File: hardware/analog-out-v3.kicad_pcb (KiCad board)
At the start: 2 copper layers, 30 x 35 mm, 41 parts, among them P1 DEBUG, P2 CONN_5, P3 CON-SENSOR2, P4 BOOT, U1 XMC1XXX24, U2 MCP4725A0, U3 TLV272IS, U4 DRILL, U5 DRILL, U6 DRILL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

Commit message: pullup 4k7->2k2, fix origin, fix logos
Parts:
- RP2: value 4k7 -> 2k2
- moved G*** 11.0 mm to (153.1, 100.1)
- moved VAL 10.6 mm to (153.1, 92.1)
- moved VAL 8.06 mm to (153.1, 108.1)
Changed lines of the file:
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@@
-(kicad_pcb (version 4) (host pcbnew 4.0.2+dfsg1-stable)
+(kicad_pcb (version 4) (host pcbnew 4.0.7-e2-6376~61~ubuntu18.04.1)
   (general
     (links 78)
     (no_connects 0)
-    (area 13.564138 81.720139 168.904861 194.555743)
+    (area 13.66415 81.720139 168.904861 194.955793)
     (thickness 1.6002)
     (drawings 23)
@@
   )
   (layers
-    (0 Vorderseite signal)
-    (31 Rückseite signal)
+    (0 Vorderseite signal hide)
+    (31 Rückseite signal hide)
     (32 B.Adhes user)
     (33 F.Adhes user)
@@
     (pad_drill 1.30048)
     (pad_to_mask_clearance 0)
-    (aux_axis_origin 138.05 117.575)
-    (grid_origin 138.05 117.575)
-    (visible_elements FFFFDFBF)
+    (aux_axis_origin 138.05 82.575)
+    (grid_origin 138.05 82.575)
+    (visible_elements FFFF9FBF)
     (pcbplotparams
       (layerselection 0x00030_80000001)
@@
   )
   (module kicad-libraries:CE_5mm (layer Rückseite)
-    (at 160.05 100.075 180)
+    (at 153.05 92.075 180)
     (fp_text reference VAL (at 0 0 180) (layer B.SilkS) hide
       (effects (font (size 0.2 0.2) (thickness 0.05)) (justify mirror))
@@
   )
   (module kicad-libraries:WEEE_7mm (layer Rückseite)
-    (at 152.05 100.075 180)
+    (at 153.05 108.075 180)
     (fp_text reference VAL (at 0 0 180) (layer B.SilkS) hide
       (effects (font (size 0.2 0.2) (thickness 0.05)) (justify mirror))
@@
       (effects (font (size 0.29972 0.29972) (thickness 0.07493)))
     )
-    (fp_text value 4k7 (at 1.01 -0.02) (layer F.Fab)
+    (fp_text value 2k2 (at 1.01 -0.02) (layer F.Fab)
       (effects (font (size 0.29972 0.29972) (thickness 0.07493)))
     )
@@
   )
   (module kicad-libraries:Logo_CoMCU (layer Rückseite)
-    (at 142.02 100.055 180)
+    (at 153.05 100.075 180)
     (fp_text reference G*** (at 0 0 180) (layer B.SilkS) hide
       (effects (font (thickness 0.3)) (justify mirror))

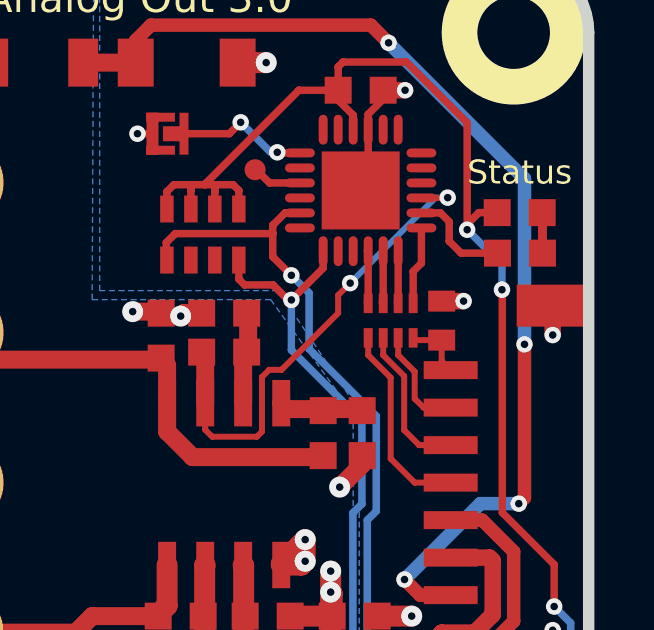
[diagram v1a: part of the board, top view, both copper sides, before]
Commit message: Change capacitor footprint(s) to C0402F
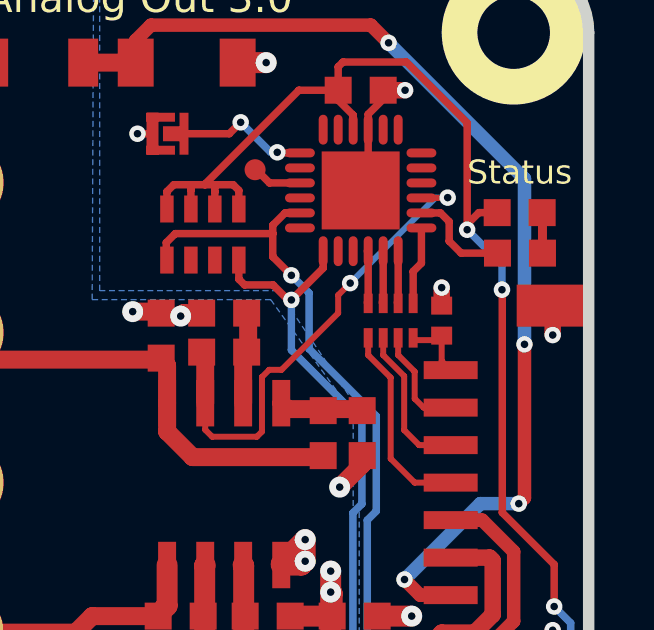
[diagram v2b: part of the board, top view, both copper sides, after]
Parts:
- C5: footprint kicad-libraries:C0402E -> kicad-libraries:C0402F
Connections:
- RP2 pad 6: (no net) -> Net-(RP2-Pad6)
- RP2 pad 7: (no net) -> Net-(RP2-Pad7)
- U1 pad 11: (no net) -> Net-(U1-Pad11)
- U1 pad 12: (no net) -> Net-(U1-Pad12)
- U1 pad 14: (no net) -> Net-(U1-Pad14)
- U1 pad 16: (no net) -> Net-(U1-Pad16)
- U1 pad 18: (no net) -> Net-(U1-Pad18)
- U1 pad 20: (no net) -> Net-(U1-Pad20)
- U1 pad 21: (no net) -> Net-(U1-Pad21)
- U1 pad 4: (no net) -> Net-(U1-Pad4)
- U1 pad 5: (no net) -> Net-(U1-Pad5)
- U1 pad 6: (no net) -> Net-(U1-Pad6)
- U1 pad 7: (no net) -> Net-(U1-Pad7)
- U1 pad 8: (no net) -> Net-(U1-Pad8)
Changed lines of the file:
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@@
-(kicad_pcb (version 4) (host pcbnew 4.0.7-e2-6376~61~ubuntu18.04.1)
+(kicad_pcb (version 4) (host pcbnew 4.0.2+dfsg1-stable)
   (general
     (links 78)
     (no_connects 0)
-    (area 13.66415 81.720139 168.904861 194.955793)
+    (area 13.564138 81.720139 168.904861 194.555743)
     (thickness 1.6002)
     (drawings 23)
@@
     (zones 0)
     (modules 41)
-    (nets 29)
+    (nets 43)
   )
   (page A4)
@@
   )
   (layers
-    (0 Vorderseite signal hide)
-    (31 Rückseite signal hide)
+    (0 Vorderseite signal)
+    (31 Rückseite signal)
     (32 B.Adhes user)
     (33 F.Adhes user)
@@
     (aux_axis_origin 138.05 82.575)
     (grid_origin 138.05 82.575)
-    (visible_elements FFFF9FBF)
+    (visible_elements FFFFDFBF)
     (pcbplotparams
       (layerselection 0x00030_80000001)
@@
   (net 27 S-CLK)
   (net 28 S-CS)
+  (net 29 "Net-(RP2-Pad6)")
+  (net 30 "Net-(RP2-Pad7)")
+  (net 31 "Net-(U1-Pad4)")
+  (net 32 "Net-(U1-Pad5)")
+  (net 33 "Net-(U1-Pad6)")
+  (net 34 "Net-(U1-Pad7)")
+  (net 35 "Net-(U1-Pad8)")
+  (net 36 "Net-(U1-Pad11)")
+  (net 37 "Net-(U1-Pad12)")
+  (net 38 "Net-(U1-Pad14)")
+  (net 39 "Net-(U1-Pad16)")
+  (net 40 "Net-(U1-Pad18)")
+  (net 41 "Net-(U1-Pad20)")
+  (net 42 "Net-(U1-Pad21)")
   (net_class Default "Dies ist die voreingestellte Netzklasse."
     (clearance 0.14986)
@@
     (add_net "Net-(R4-Pad2)")
     (add_net "Net-(R5-Pad1)")
+    (add_net "Net-(RP2-Pad6)")
+    (add_net "Net-(RP2-Pad7)")
+    (add_net "Net-(U1-Pad11)")
+    (add_net "Net-(U1-Pad12)")
+    (add_net "Net-(U1-Pad14)")
+    (add_net "Net-(U1-Pad16)")
+    (add_net "Net-(U1-Pad18)")
+    (add_net "Net-(U1-Pad20)")
+    (add_net "Net-(U1-Pad21)")
+    (add_net "Net-(U1-Pad4)")
+    (add_net "Net-(U1-Pad5)")
+    (add_net "Net-(U1-Pad6)")
+    (add_net "Net-(U1-Pad7)")
+    (add_net "Net-(U1-Pad8)")
     (add_net S-CLK)
     (add_net S-CS)
@@
     (pad 3 smd oval (at -2.025 -0.25 180) (size 1 0.3) (layers Vorderseite F.Paste F.Mask)
       (net 20 VIN))
-    (pad 4 smd oval (at -2.025 0.25 180) (size 1 0.3) (layers Vorderseite F.Paste F.Mask))
-    (pad 5 smd oval (at -2.025 0.75 180) (size 1 0.3) (layers Vorderseite F.Paste F.Mask))
-    (pad 6 smd oval (at -2.025 1.25 180) (size 1 0.3) (layers Vorderseite F.Paste F.Mask))
-    (pad 7 smd oval (at -1.25 2.025 270) (size 1 0.3) (layers Vorderseite F.Paste F.Mask))
-    (pad 8 smd oval (at -0.75 2.025 270) (size 1 0.3) (layers Vorderseite F.Paste F.Mask))
+    (pad 4 smd oval (at -2.025 0.25 180) (size 1 0.3) (layers Vorderseite F.Paste F.Mask)
+      (net 31 "Net-(U1-Pad4)"))
+    (pad 5 smd oval (at -2.025 0.75 180) (size 1 0.3) (layers Vorderseite F.Paste F.Mask)
+      (net 32 "Net-(U1-Pad5)"))
+    (pad 6 smd oval (at -2.025 1.25 180) (size 1 0.3) (layers Vorderseite F.Paste F.Mask)
+      (net 33 "Net-(U1-Pad6)"))
+    (pad 7 smd oval (at -1.25 2.025 270) (size 1 0.3) (layers Vorderseite F.Paste F.Mask)
+      (net 34 "Net-(U1-Pad7)"))
+    (pad 8 smd oval (at -0.75 2.025 270) (size 1 0.3) (layers Vorderseite F.Paste F.Mask)
+      (net 35 "Net-(U1-Pad8)"))
     (pad 9 smd oval (at -0.25 2.025 270) (size 1 0.3) (layers Vorderseite F.Paste F.Mask)
       (net 2 GND))
     (pad 10 smd oval (at 0.25 2.025 270) (size 1 0.3) (layers Vorderseite F.Paste F.Mask)
       (net 7 3V3))
-    (pad 11 smd oval (at 0.75 2.025 270) (size 1 0.3) (layers Vorderseite F.Paste F.Mask))
-    (pad 12 smd oval (at 1.25 2.025 270) (size 1 0.3) (layers Vorderseite F.Paste F.Mask))
+    (pad 11 smd oval (at 0.75 2.025 270) (size 1 0.3) (layers Vorderseite F.Paste F.Mask)
+      (net 36 "Net-(U1-Pad11)"))
+    (pad 12 smd oval (at 1.25 2.025 270) (size 1 0.3) (layers Vorderseite F.Paste F.Mask)
+      (net 37 "Net-(U1-Pad12)"))
     (pad 13 smd oval (at 2.025 1.25 180) (size 1 0.3) (layers Vorderseite F.Paste F.Mask)
       (net 19 "Net-(P4-Pad2)"))
-    (pad 14 smd oval (at 2.025 0.75 180) (size 1 0.3) (layers Vorderseite F.Paste F.Mask))
+    (pad 14 smd oval (at 2.025 0.75 180) (size 1 0.3) (layers Vorderseite F.Paste F.Mask)
+      (net 38 "Net-(U1-Pad14)"))
     (pad 15 smd oval (at 2.025 0.25 180) (size 1 0.3) (layers Vorderseite F.Paste F.Mask)
       (net 18 "Net-(P1-Pad1)"))
-    (pad 16 smd oval (at 2.025 -0.25 180) (size 1 0.3) (layers Vorderseite F.Paste F.Mask))
+    (pad 16 smd oval (at 2.025 -0.25 180) (size 1 0.3) (layers Vorderseite F.Paste F.Mask)
+      (net 39 "Net-(U1-Pad16)"))
     (pad 17 smd oval (at 2.025 -0.75 180) (size 1 0.3) (layers Vorderseite F.Paste F.Mask)
       (net 4 SDA))
-    (pad 18 smd oval (at 2.025 -1.25 180) (size 1 0.3) (layers Vorderseite F.Paste F.Mask))
+    (pad 18 smd oval (at 2.025 -1.25 180) (size 1 0.3) (layers Vorderseite F.Paste F.Mask)
+      (net 40 "Net-(U1-Pad18)"))
     (pad 19 smd oval (at 1.25 -2.025 270) (size 1 0.3) (layers Vorderseite F.Paste F.Mask)
       (net 3 SCL))
-    (pad 20 smd oval (at 0.75 -2.025 270) (size 1 0.3) (layers Vorderseite F.Paste F.Mask))
-    (pad 21 smd oval (at 0.25 -2.025 270) (size 1 0.3) (layers Vorderseite F.Paste F.Mask))
+    (pad 20 smd oval (at 0.75 -2.025 270) (size 1 0.3) (layers Vorderseite F.Paste F.Mask)
+      (net 41 "Net-(U1-Pad20)"))
+    (pad 21 smd oval (at 0.25 -2.025 270) (size 1 0.3) (layers Vorderseite F.Paste F.Mask)
+      (net 42 "Net-(U1-Pad21)"))
     (pad 22 smd oval (at -0.25 -2.025 270) (size 1 0.3) (layers Vorderseite F.Paste F.Mask)
       (net 28 S-CS))
@@
     )
   )
-  (module kicad-libraries:C0402E (layer Vorderseite)
-    (at 163.15 94.675 90)
-    (attr smd)
-    (fp_text reference C5 (at 0 0.125 90) (layer F.Fab)
-      (effects (font (size 0.2 0.2) (thickness 0.05)))
-    )
-    (fp_text value 220pF (at 0 -0.275 90) (layer F.Fab)
-      (effects (font (size 0.2 0.2) (thickness 0.05)))
-    )
-    (fp_line (start -0.8509 -0.44958) (end 0.8509 -0.44958) (layer F.Fab) (width 0.001))
-    (fp_line (start 0.8509 -0.44958) (end 0.8509 0.44958) (layer F.Fab) (width 0.001))
-    (fp_line (start 0.8509 0.44958) (end -0.8509 0.44958) (layer F.Fab) (width 0.001))
-    (fp_line (start -0.8509 0.44958) (end -0.8509 -0.44958) (layer F.Fab) (width 0.001))
-    (pad 1 smd rect (at -0.65 0 90) (size 0.7 0.9) (layers Vorderseite F.Paste F.Mask)
-      (net 16 "Net-(C5-Pad1)"))
-    (pad 2 smd rect (at 0.65 0 90) (size 0.7 0.9) (layers Vorderseite F.Paste F.Mask)
-      (net 2 GND))
-    (model Capacitors_SMD/C_0402.wrl
-      (at (xyz 0 0 0))
-      (scale (xyz 1 1 1))
-      (rotate (xyz 0 0 0))
-    )
-  )
   (module kicad-libraries:R0603F (layer Vorderseite)
     (at 159.2 98.425 90)
@@
     (pad 5 smd rect (at 1.19888 0.8509) (size 0.44958 0.89916) (layers Vorderseite F.Paste F.Mask)
       (net 3 SCL))
-    (pad 6 smd rect (at 0.39878 0.8509) (size 0.44958 0.89916) (layers Vorderseite F.Paste F.Mask))
-    (pad 7 smd rect (at -0.39878 0.8509) (size 0.44958 0.89916) (layers Vorderseite F.Paste F.Mask))
+    (pad 6 smd rect (at 0.39878 0.8509) (size 0.44958 0.89916) (layers Vorderseite F.Paste F.Mask)
+      (net 29 "Net-(RP2-Pad6)"))
+    (pad 7 smd rect (at -0.39878 0.8509) (size 0.44958 0.89916) (layers Vorderseite F.Paste F.Mask)
+      (net 30 "Net-(RP2-Pad7)"))
     (pad 8 smd rect (at -1.19888 0.8509) (size 0.44958 0.89916) (layers Vorderseite F.Paste F.Mask)
       (net 4 SDA))
@@
       (clearance 0.65024))
   )
+  (module kicad-libraries:C0402F (layer Vorderseite)
+    (at 163.15 94.675 90)
+    (fp_text reference C5 (at 0.1 0.15 90) (layer F.Fab)
+      (effects (font (size 0.2 0.2) (thickness 0.05)))
+    )
+    (fp_text value 220pF (at 0 -0.15 90) (layer F.Fab)
+      (effects (font (size 0.2 0.2) (thickness 0.05)))
+    )
+    (fp_line (start -0.9 -0.45) (end 0.9 -0.45) (layer F.Fab) (width 0.025))
+    (fp_line (start 0.9 -0.45) (end 0.9 0.45) (layer F.Fab) (width 0.025))
+    (fp_line (start 0.9 0.45) (end -0.9 0.45) (layer F.Fab) (width 0.025))
+    (fp_line (start -0.9 0.45) (end -0.9 -0.45) (layer F.Fab) (width 0.025))
+    (pad 2 smd rect (at 0.5 0 90) (size 0.6 0.7) (layers Vorderseite F.Paste F.Mask)
+      (net 2 GND))
+    (pad 1 smd rect (at -0.5 0 90) (size 0.6 0.7) (layers Vorderseite F.Paste F.Mask)
+      (net 16 "Net-(C5-Pad1)"))
+    (model Capacitors_SMD/C_0402.wrl
+      (at (xyz 0 0 0))
+      (scale (xyz 1 1 1))
+      (rotate (xyz 0 0 0))
+    )
+  )
   (gr_text Status (at 165.75 89.735) (layer F.SilkS)
     (effects (font (size 0.8 0.8) (thickness 0.15)))
@@
   (segment (start 152.95074 86.075) (end 152.95074 85.33426) (width 0.45) (layer Vorderseite) (net 1))
   (segment (start 152.95074 86.075) (end 151.20114 86.075) (width 0.59944) (layer Vorderseite) (net 1))
+  (segment (start 163.15 94.175) (end 163.15 93.575) (width 0.55) (layer Vorderseite) (net 2))
+  (via (at 163.15 93.575) (size 0.55) (drill 0.25) (layers Vorderseite Rückseite) (net 2))
   (segment (start 153.51 88.445) (end 153.01 88.445) (width 0.25) (layer Vorderseite) (net 2))
   (via (at 153.01 88.445) (size 0.55) (drill 0.25) (layers Vorderseite Rückseite) (net 2))
@@
   (segment (start 160.7 87.795) (end 161.2 87.295) (width 0.25) (layer Vorderseite) (net 2))
   (segment (start 161.2 87.295) (end 161.2 86.995) (width 0.25) (layer Vorderseite) (net 2))
-  (segment (start 163.15 94.025) (end 163.88 94.025) (width 0.55) (layer Vorderseite) (net 2))
-  (via (at 163.88 94.025) (size 0.55) (drill 0.25) (layers Vorderseite Rückseite) (net 2))
   (segment (start 166.85 105.975) (end 166.85 104.995) (width 0.55) (layer Vorderseite) (net 2))
   (via (at 166.85 104.995) (size 0.55) (drill 0.25) (layers Vorderseite Rückseite) (net 2))

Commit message: specify processor
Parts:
- U1: value XMC1XXX24 -> XMC11XX24
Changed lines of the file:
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@@
-(kicad_pcb (version 4) (host pcbnew 4.0.2+dfsg1-stable)
+(kicad_pcb (version 4) (host pcbnew 4.0.7-e2-6376~61~ubuntu18.04.1)
   (general
     (links 78)
     (no_connects 0)
-    (area 13.564138 81.720139 168.904861 194.555743)
+    (area 13.66415 81.720139 168.904861 194.955793)
     (thickness 1.6002)
     (drawings 23)
@@
       (effects (font (size 0.3 0.3) (thickness 0.075)))
     )
-    (fp_text value XMC1XXX24 (at 0 0.8 180) (layer F.Fab)
+    (fp_text value XMC11XX24 (at 0 0.8 180) (layer F.Fab)
       (effects (font (size 0.3 0.3) (thickness 0.075)))
     )

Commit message: specify processor as XMC1100
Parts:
- U1: value XMC11XX24 -> XMC1100
